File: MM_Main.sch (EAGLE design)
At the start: 68 parts, among them IC1 ULN2003AD, IC2 TB6612FNG, IC3 FXAS21002C, IC4 LD117ADT50TR, Q1 TEFT4300, Q2 TEFT4300, Q3 TEFT4300, Q4 TEFT4300, Q7 8MHz, Q8 32,768kHz

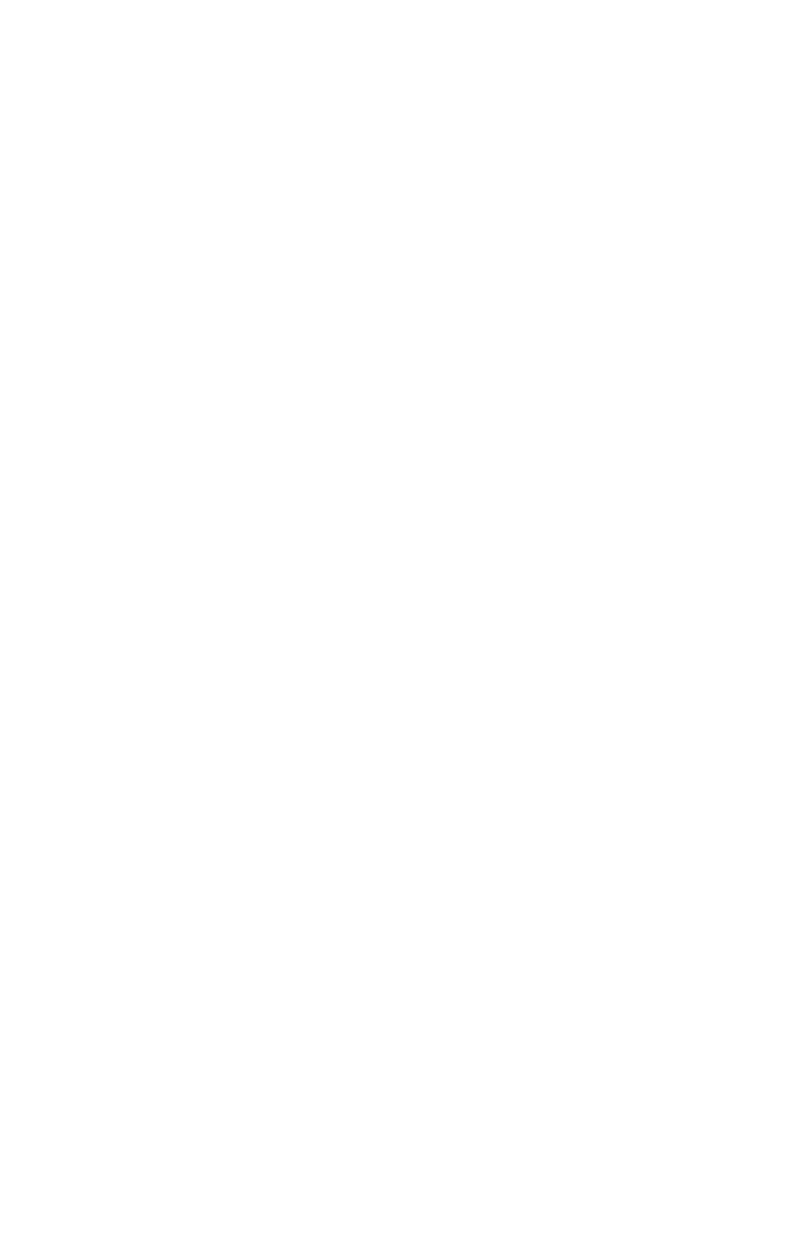
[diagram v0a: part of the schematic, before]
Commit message: dodanie stm32f4 do lib
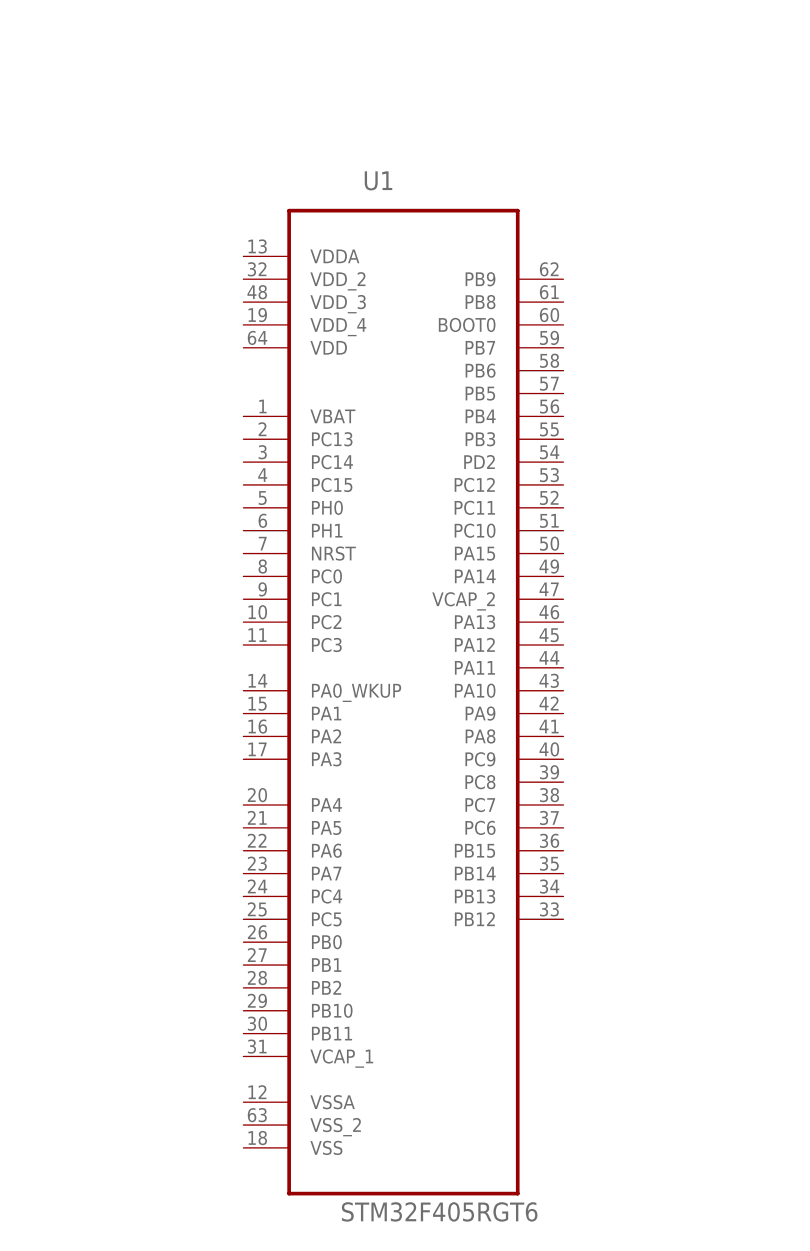
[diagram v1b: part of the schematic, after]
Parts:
- added U1: STM32F405RGT6, _microMouse:STM32F405RGT6
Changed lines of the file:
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@@
 <?xml version="1.0" encoding="utf-8"?>
 <!DOCTYPE eagle SYSTEM "eagle.dtd">
-<eagle version="7.1.0">
+<eagle version="7.2.0">
 <drawing>
 <settings>
@@
 <part name="C16" library="rcl" deviceset="CPOL-EU" device="SMCA" value="tant-a-4,7u"/>
 <part name="C13" library="rcl" deviceset="CPOL-EU" device="SMCA" value="tant-a-10u"/>
+<part name="U1" library="_microMouse" deviceset="STM32F405RGT6" device=""/>
 </parts>
 <sheets>
@@
 </instance>
 <instance part="C13" gate="G$1" x="-53.34" y="-20.32"/>
+<instance part="U1" gate="A" x="208.28" y="-17.78"/>
 </instances>
 <busses>

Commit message: dodanie wymiarowania do gyro i zepsucie termali :P
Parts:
- removed BT, PROG: (no value), pinhead:PINHD-1X4
- removed C10, C18, C3, C4, C7, C9: 100n, rcl:C-EUC0603
- removed C5, C8: tant-a-4u7, rcl:CPOL-EUSMCA
- removed C_OSC3, C_OSC4: 10p, rcl:C-EUC0805
- removed F1: (no value), fuse:GSH15
- removed IC3: FXAS21002C, _microMouse:FXAS21002C
- removed M_L, M_R: (no value), pinhead:PINHD-1X3
- removed Q8: 32,768kHz, crystal:CRYSTALHC49U70
- removed U$3: TACTILE-SWITCH-7914G, GeekAmmo:TACTILE-SWITCH-7914G
- added BAT: (no value), pinhead:PINHD-1X3
- added BT-PROG: (no value), con-ml:ML10
- added BTN1, RST_BTN: TACTILE-SWITCH-7914G, GeekAmmo:TACTILE-SWITCH-7914G
- added D5, D6: SFH4545, _microMouse:SFH4545
- added FUSE, FUSE1: (no value), resistor:R-EU_M2012
- added L1, L2: LABITYNT, _microMouse:LABITYNT
- added LED3: yellow, led:LEDSML1206
- added Q5, Q6: TEFT4300, _MM:TEFT4300
- added R17: (no value), resistor:R-EU_R0805
- added R18, R19, R20, R22, R23, R24, R25: (no value), rcl:R-EU_R0805
- added R21: 10k...47k, rcl:R-EU_R0805
- added S1: (no value), switch:255SB
- added SG2: F/QMX, buzzer:F/QMX
- added U$5: MOTOR_MOUNT, _microMouse:MOTOR_MOUNT
- C1, C2: device rcl:C-EUC0603 -> rcl:C-EUC0805
- LED1: value (none) -> red
- LED2: value (none) -> green
- Q7: device crystal:CRYSTALHC49U70 -> crystal:CRYSTALCTS406
- R10: value 10k -> 10K
- R9: device rcl:R-EU_R0805 -> resistor:R-EU_R0805
- U$1: value STM32F103_LQFP48 -> 9AXIS_MODULE; device STM32F10x F4xx:STM32F103_LQFP48 -> _microMouse:9AXIS_MODULE
- U$2: value FXOS8700CQR1 -> LI-POL-DUALKSY_220MAH_D; device _microMouse:FXOS8700CQR1 -> _microMouse:LI-POL-DUALKSY_220MAH_D
- ZAS: device pinhead:PINHD-1X3 -> special:SW_DIP-1
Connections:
- removed net 5V: C21.+, IC4.OUT, U$4.IN, U$4.SHDN
- removed net BUTTON: R11.1, U$1.PA0-WKUP
- removed net GND3: C18.2, C8.-, IC3.GND3
- removed net LED: LED2.C
- removed net M_L_IN1: IC2.AIN2, U$1.PB5
- removed net M_L_IN2: IC2.AIN1, U$1.PB4
- removed net M_L_PWM: IC2.PWMA, U$1.PB7
- removed net M_R_IN1: IC2.BIN1, U$1.PB3
- removed net M_R_IN2: IC2.BIN2, U$1.PA15
- removed net M_R_PWM: IC2.PWMB, U$1.PB6
- removed net N$2: C7.2, R10.1, U$1.NRST
- removed net N$26: C10.1, IC3.VREGD
- removed net N$27: IC3.PWR_CTRL
- removed net N$28: IC3.INT1
- removed net N$30: IC3.RST_B, R9.1
- removed net OSC32_IN: C_OSC3.2, Q8.2, U$1.PC14-OSC32_IN
- removed net OSC32_OUT: C_OSC4.2, Q8.1, U$1.PC15-OSC_OUT
- removed net VBAT: C22.+, IC4.IN, U$3.3
- removed net VCC: IC3.I2C_B/SPI
- removed net VDD: IC3.VDD
- removed net VDDA: C14.2, C16.-, U$1.VDDA
- removed net VDDIO: C9.2, IC3.VDDIO
- removed net VSSA: C14.1, C16.+, U$1.VSSA
- new net +5V: C21.+, IC4.OUT, U$4.IN, U$4.SHDN, U$5.L_VCC, U$5.R_VCC
- new net ADC: Q5.E, R23.2, U1.PB0
- new net ADC2: Q6.E, R24.2, U1.PC5
- new net ADC_VBAT: R17.2, R9.1, U1.PB1
- new net BOOT0: R18.1, U1.BOOT0
- new net BTN: BTN1.3, R20.2, U1.PB2
- new net BUZZER: IC1.I7, U1.PB8
- new net CS_A: U$1.CS_A
- new net D_LL: IC1.I2, U1.PC13
- new net D_RR: IC1.I4, U1.PC14
- new net ENCL_A: U$5.L_CHA, U1.PA6
- new net ENCL_B: U$5.L_CHB, U1.PA7
- new net ENCR_A: U$5.R_CHA, U1.PA0_WKUP
- new net ENCR_B: U$5.R_CHB, U1.PA1
- new net ML_IN1: IC2.AIN2, U1.PC6
- new net ML_IN2: IC2.AIN1, U1.PC7
- new net ML_PWM: IC2.PWMA, U1.PB14
- new net MR_IN1: IC2.BIN1, U1.PC8
- new net MR_IN2: IC2.BIN2, U1.PC9
- new net MR_PWM: IC2.PWMB, U1.PB15
- new net N$22: IC1.O7, SG2.1
- new net N$23: R18.2, R19.2, S1.P
- new net N$3: D5.C, IC1.O2
- new net N$5: D5.A, R22.1
- new net N$8: LED3.A, R10.1
- new net RST: C2.1, R21.1, RST_BTN.1, U1.NRST
- net +3V3: now also BT-PROG.3, BT-PROG.4, C14.1, C16.+, Q5.C, Q6.C, R11.1, R21.2, S1.O, U$1.+3V3, U1.VBAT, U1.VSS, U1.VSSA, U1.VSS_2; no longer BT.4, C18.1, C3.1, C4.2, C5.+, C8.+, PROG.1, R9.2, U$1.VBAT, U$2.VDD, U$2.VDDIO
- net +7V: now also C1.1, C22.+, FUSE.1, FUSE1.1, IC1.CD+, IC4.IN, R22.2, R25.1, R9.2, SG2.2; no longer F1.2
- net ADC_L: now also U1.PC1; no longer U$1.PA2
- net ADC_LF: now also U1.PC0; no longer U$1.PA1
- net ADC_R: now also U1.PC2; no longer U$1.PA3
- net ADC_RF: now also U1.PC3; no longer U$1.PA4
- net BT_RXD: now also BT-PROG.9, U1.PA9; no longer BT.1, U$1.PA9
- net BT_TXD: now also BT-PROG.7, U1.PA10; no longer BT.2, U$1.PA10
- net CS_G: now also U$1.CS_G; no longer U$2.SA1/CS_B
- net D_L: now also U1.PB3; no longer IC1.I4, U$1.PB1
- net D_LF: now also U1.PD2; no longer IC1.I2, U$1.PB0
- net D_R: now also U1.PB4; no longer IC1.I6, U$1.PB10
- net D_RF: now also U1.PB5; no longer IC1.I7, U$1.PB11
- net GND: now also BT-PROG.5, BT-PROG.6, C14.2, C16.-, C2.2, R17.1, R19.1, R20.1, R23.1, R24.1, RST_BTN.3, U$1.GND, U$5.L_GND, U$5.R_GND, U1.VDD, U1.VDDA, U1.VDD_2, U1.VDD_3, U1.VDD_4; no longer BT.3, C1.2, C10.2, C2.1, C3.2, C4.1, C5.-, C6.-, C7.1, C9.1, C_OSC3.1, C_OSC4.1, IC1.GND, IC3.GND1, IC3.GND2, IC3.GND4, IC3.RGND, IC3.RGND1, IC3.RGND2, IC3.RGND3, IC3.RGND4, IC3.RGND5, IC3.RGND6, IC3.RGND7, IC3.RGND8, PROG.2, U$2.GND, U$2.GND., U$2.NC-GND, U$2.NC-GND., U$2.RST
- net GNDA: now also C1.2, C6.-, IC1.GND, ZAS.2; no longer ZAS.1, ZAS.3
- net INT_G: now also U$1.INT_G; no longer U$2.INT1
- net LED1: now also LED2.C, U1.PA12; no longer U$1.PB9
- net LED2: now also LED3.C, U1.PA11; no longer U$1.PB8
- net MISO: now also U$1.MISO, U1.PC11; no longer IC3.SA0/MISO, U$1.PB14, U$2.SA0/MISO
- net MOSI: now also U$1.MOSI, U1.PC12; no longer IC3.SDA/MOSI, U$1.PB15, U$2.SDA/MOSI
- net N$13: no longer IC1.O2
- net N$14: no longer IC1.O4
- net N$15: no longer IC1.O6
- net N$16: now also IC1.O6; no longer IC1.O7
- net N$18: now also U$5.R_MOTOR_B; no longer M_L.2
- net N$19: now also U$5.L_MOTOR_B; no longer M_R.1, M_R.3
- net N$20: now also U$5.L_MOTOR_A; no longer M_R.2
- net N$24: now also BAT.2, FUSE.2, FUSE1.2; no longer F1.1, ZAS.2
- net N$25: now also BAT.1, BAT.3, ZAS.1; no longer IC3.SPI_CS_B
- net N$29: now also BTN1.1; no longer U$3.1
- net N$31: no longer U$1.BOOT0
- net N$33: no longer U$1.PB2
- net N$6: now also D6.C, IC1.O4; no longer C1.1, U$2.C-RST
- net N$7: now also D6.A, R25.2; no longer C2.2, U$2.BYP
- net N$9: now also U$5.R_MOTOR_A; no longer M_L.1, M_L.3
- net OSC_IN: now also U1.PH0; no longer U$1.PD0-OSC_IN
- net OSC_OUT: now also U1.PH1; no longer U$1.PD1-OSC_OUT
- net SCK: now also U1.PC10; no longer U$1.PB13
- net SCLK: now also U$1.SCLK; no longer IC3.SCL/SCLK, U$2.SCL/SCLK
- net SWCLK: now also BT-PROG.10, U1.PA14; no longer PROG.4, U$1.PA14
- net SWDIO: now also BT-PROG.8, U1.PA13; no longer PROG.3, U$1.PA13
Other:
- note added: "Boot1"
- note added: "Dobrać obudowę buzzera"
- note added: "Tu jest +5V"
- note added: "VSSA"
- note added: "dobrać gniazda do bat"
- note added: "dobrać obudowę bezpiecznika i switcha zasilania"
- note added: "też bootloader"
- note removed: "Note: Pullup resistors on INT1 and INT2 are not required if these pins are configured for push/pull (default) operation."
- note removed: "Note: Pullup resistors on SCL/SCLK and SDA/MOSI are not required if the device is operated in SPI Interface mode."
- note removed: "RST - Connect to GND if unused"
- note removed: "RST_B - Connect to VDDIO if unused"
- note removed: "VDDIO (1.62 to VDD + 0.3 V)"
- note removed: "ZMIENIC OBUDOWE KWARCU Q8"
- moved on the sheet: C1, C2, R10, R11, R9, U1

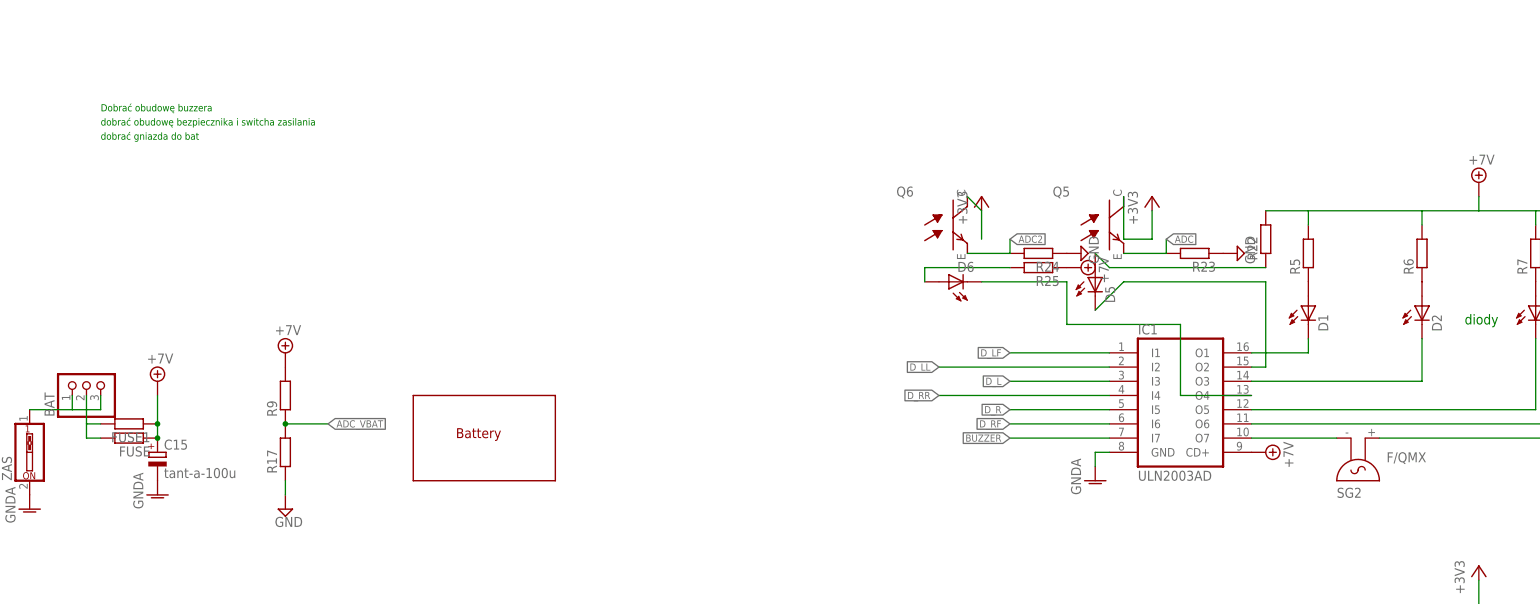
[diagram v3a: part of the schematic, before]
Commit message: dodany buzzer w lbr i sch
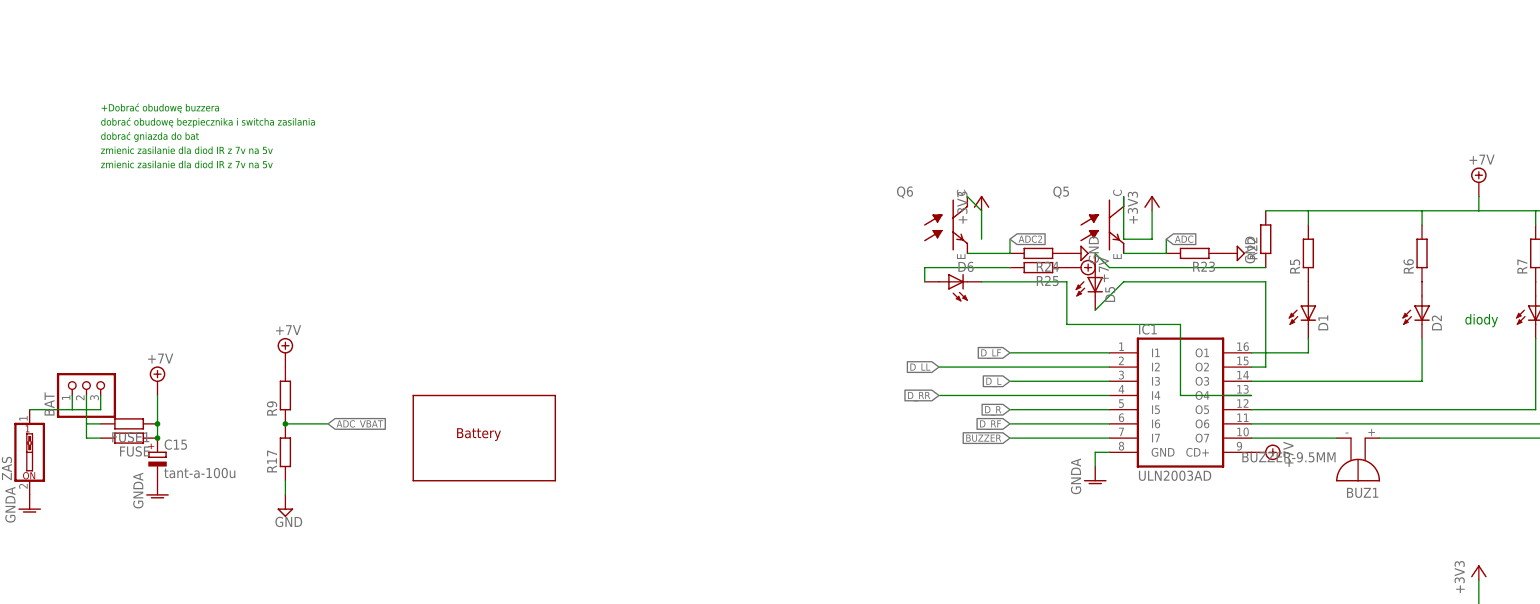
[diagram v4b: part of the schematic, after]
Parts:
- removed SG2: F/QMX, buzzer:F/QMX
- added BUZ1: BUZZER-9.5MM, _microMouse:BUZZER-9.5MM
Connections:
- net +7V: now also BUZ1.+; no longer SG2.2
- net N$22: now also BUZ1.-; no longer SG2.1
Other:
- note added: "+Dobrać obudowę buzzera"
- note added: "zmienic zasilanie dla diod IR z 7v na 5v"
- note removed: "Dobrać obudowę buzzera"
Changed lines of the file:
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@@
 <part name="+3V20" library="supply1" deviceset="+3V3" device=""/>
 <part name="ZAS" library="special" deviceset="SW_DIP-1" device=""/>
-<part name="SG2" library="buzzer" deviceset="F/QMX" device=""/>
 <part name="S1" library="switch" deviceset="255SB" device=""/>
 <part name="FUSE" library="resistor" deviceset="R-EU_" device="M2012"/>
@@
 <part name="GND2" library="supply1" deviceset="GNDA" device=""/>
 <part name="GND3" library="supply1" deviceset="GNDA" device=""/>
+<part name="BUZ1" library="_microMouse" deviceset="BUZZER-9.5MM" device=""/>
 </parts>
 <sheets>
@@
 <text x="-116.84" y="2.54" size="1.778" layer="97">DO ENKODEROW</text>
 <text x="-109.22" y="22.86" size="1.27" layer="91">Tu jest +5V</text>
-<text x="-139.7" y="180.34" size="1.27" layer="91">Dobrać obudowę buzzera</text>
+<text x="-139.7" y="180.34" size="1.27" layer="91">+Dobrać obudowę buzzera</text>
 <text x="-139.7" y="177.8" size="1.27" layer="91">dobrać obudowę bezpiecznika i switcha zasilania</text>
 <text x="-139.7" y="175.26" size="1.27" layer="91">dobrać gniazda do bat</text>
@@
 <text x="167.64" y="-53.34" size="1.27" layer="91" rot="R180">Boot1</text>
 <text x="7.62" y="35.56" size="1.27" layer="91">VSSA</text>
+<text x="-139.7" y="172.72" size="1.27" layer="91">zmienic zasilanie dla diod IR z 7v na 5v</text>
+<text x="-139.7" y="170.18" size="1.27" layer="91">zmienic zasilanie dla diod IR z 7v na 5v</text>
 </plain>
 <instances>
@@
 <instance part="+3V20" gate="G$1" x="-68.58" y="76.2"/>
 <instance part="ZAS" gate="G$1" x="-152.4" y="119.38" rot="R90"/>
-<instance part="SG2" gate="G$1" x="83.82" y="119.38" rot="MR180"/>
 <instance part="S1" gate="1" x="289.56" y="22.86"/>
 <instance part="FUSE" gate="G$1" x="-134.62" y="121.92" rot="R180"/>
@@
 <instance part="GND2" gate="1" x="160.02" y="124.46"/>
 <instance part="GND3" gate="1" x="175.26" y="124.46"/>
+<instance part="BUZ1" gate="G$1" x="85.09" y="118.872" rot="R180"/>
 </instances>
 <busses>
@@
 <wire x1="175.26" y1="162.56" x2="175.26" y2="147.32" width="0.1524" layer="91"/>
 <pinref part="C1" gate="G$1" pin="1"/>
-<pinref part="SG2" gate="G$1" pin="2"/>
 <wire x1="76.2" y1="162.56" x2="68.58" y2="162.56" width="0.1524" layer="91"/>
 <pinref part="R22" gate="G$1" pin="2"/>
+<pinref part="BUZ1" gate="G$1" pin="+"/>
 </segment>
 <segment>
@@
 <pinref part="IC1" gate="A" pin="O7"/>
 <wire x1="66.04" y1="121.92" x2="81.28" y2="121.92" width="0.1524" layer="91"/>
-<pinref part="SG2" gate="G$1" pin="1"/>
-</segment>
-</net>
+<pinref part="BUZ1" gate="G$1" pin="-"/>
+</segment>
+</net>

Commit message: wszystkie sciezki polaczone \!
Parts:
- removed C_V3: 100n, rcl:C-EUC0805
- removed R14, R15: 47k, resistor:R-EU_R0805
- added BAT1, BOOT: (no value), pinhead:PINHD-1X3
- added S2: (no value), adafruit:EG1218S
- BUZ1: value BUZZER-9.5MM -> BUZZER-9.5MM-3V?
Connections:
- removed net N$31: R14.1
- removed net N$33: R15.2
- removed net VDD1: C_V1.1
- removed net VDD2: C_V2.1
- removed net VDD3: C_V3.1
- removed net VSS1: C_V1.2
- removed net VSS2: C_V2.2
- removed net VSS3: C_V3.2
- net +3V3: now also C_V1.1, C_V2.1
- net +5V: now also BT-PROG.1, BT-PROG.2, BUZ1.+, C1.1, C6.+, IC1.CD+, R22.2, R25.1, R5.2, R6.2, R7.2, R8.2
- net +7V: no longer BUZ1.+, C1.1, C6.+, IC1.CD+, R22.2, R25.1, R5.2, R6.2, R7.2, R8.2
- net GND: now also C_V1.2, C_V2.2; no longer R14.2, R15.1
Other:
- note added: "Vdd1"
- note added: "połączyć masy"
- note added: "vdd2"
- note removed: "+Dobrać obudowę buzzera"
- note removed: "dobrać gniazda do bat"
- note removed: "dobrać obudowę bezpiecznika i switcha zasilania"
- note removed: "zmienic zasilanie dla diod IR z 7v na 5v"

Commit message: renament - 4 LED + all on top
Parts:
- removed BT-PROG: (no value), con-ml:ML10
- removed D5, D6: SFH4545, _microMouse:SFH4545
- removed Q5, Q6: TEFT4300, _MM:TEFT4300
- removed R22, R23, R24, R25: (no value), rcl:R-EU_R0805
- removed S2: (no value), adafruit:EG1218S
- added JP1: (no value), pinhead:PINHD-2X4
- D1, D2, D3, D4: value SFH4545 -> SFH4545-C; device _microMouse:SFH4545 -> _microMouse:SFH4545-C
- renumbered C14 to C_VSSA, C16 to C_VSSA2
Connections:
- removed net ADC: Q5.E, R23.2, U1.PB0
- removed net ADC2: Q6.E, R24.2, U1.PC5
- removed net INT_G: U$1.INT_G
- removed net N$20: IC2.BO1, IC2.BO1', U$5.L_MOTOR_A
- removed net N$22: BUZ1.-, IC1.O7
- removed net N$25: BAT.1, BAT.3, ZAS.1
- removed net N$3: D5.C, IC1.O2
- removed net SCK: U1.PC10
- new net INT_A: U$1.INT_G, U1.PB5
- new net N$30: U1.PA8
- new net N$32: U1.VCAP_2
- new net N$34: U1.PA15
- new net N$35: U1.PD2
- new net N$36: U1.PB8
- new net N$37: U1.PB9
- new net N$38: U1.PB13
- new net N$39: U1.PB12
- new net N$40: U1.PC4
- new net N$41: U1.PC5
- net +3V3: now also JP1.7, JP1.8; no longer BT-PROG.3, BT-PROG.4, Q5.C, Q6.C
- net +5V: no longer BT-PROG.1, BT-PROG.2, R22.2, R25.1
- net BTN: now also U1.PB0; no longer U1.PB2
- net BT_RXD: now also JP1.1; no longer BT-PROG.9
- net BT_TXD: now also JP1.3; no longer BT-PROG.7
- net BUZZER: now also U1.PA5; no longer U1.PB8
- net CS_A: now also U1.PB4
- net CS_G: now also U1.PB3
- net D_L: now also U1.PA2; no longer U1.PB3
- net D_LF: now also U1.PA1; no longer U1.PD2
- net D_LL: no longer IC1.I2
- net D_R: now also U1.PA3; no longer U1.PB4
- net D_RF: now also IC1.I6, U1.PA4; no longer U1.PB5
- net D_RR: no longer IC1.I4
- net ENCR_A: now also U1.PB6; no longer U1.PA0_WKUP
- net ENCR_B: now also U1.PB7; no longer U1.PA1
- net GND: now also JP1.5, JP1.6; no longer BT-PROG.5, BT-PROG.6, R23.1, R24.1
- net GNDA: now also BAT.1, BAT.3; no longer ZAS.2
- net N$15: now also IC1.O7; no longer IC1.O5
- net N$18: now also U$5.L_MOTOR_B; no longer U$5.R_MOTOR_B
- net N$19: now also BUZ1.-, IC1.O5; no longer IC2.BO2, IC2.BO2', U$5.L_MOTOR_B
- net N$24: now also ZAS.2; no longer BAT.2
- net N$5: now also IC2.BO2, IC2.BO2', U$5.R_MOTOR_B; no longer D5.A, R22.1
- net N$6: now also IC2.BO1, IC2.BO1', U$5.R_MOTOR_A; no longer D6.C, IC1.O4
- net N$7: now also IC2.AO1, IC2.AO1', U$5.L_MOTOR_A; no longer D6.A, R25.2
- net N$9: now also BAT.2, ZAS.1; no longer IC2.AO1, IC2.AO1', U$5.R_MOTOR_A
- net SCLK: now also U1.PC10
- net SWCLK: now also JP1.2; no longer BT-PROG.10
- net SWDIO: now also JP1.4; no longer BT-PROG.8
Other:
- moved on the sheet: BAT, BUZ1, C15, FUSE, FUSE1, ZAS
